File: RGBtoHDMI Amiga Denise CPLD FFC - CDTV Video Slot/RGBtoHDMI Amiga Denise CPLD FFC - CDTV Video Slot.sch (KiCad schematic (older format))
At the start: 33 parts, among them CN10 Conn_02x15_Odd_Even, J1 Raspberry_Pi_2_3, U1 XC9572VQ44 or XC9572XL-10VQG4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

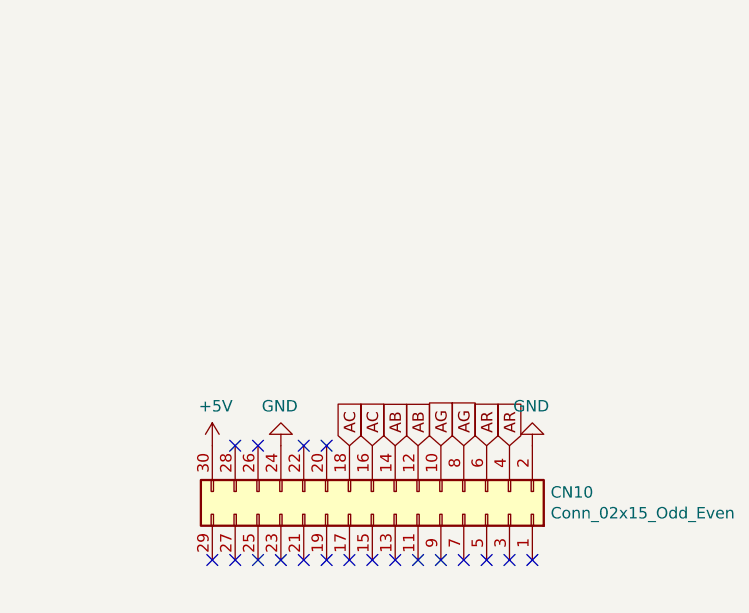
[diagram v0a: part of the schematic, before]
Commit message: Added L+R audio points
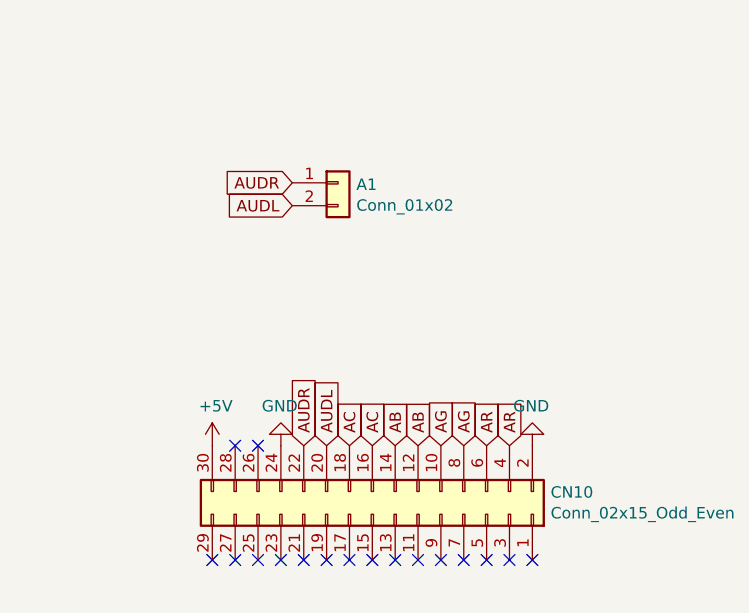
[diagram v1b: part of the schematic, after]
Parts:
- added A1: Conn_01x02, Connector_PinHeader_2.54mm:PinHeader_1x02_P2.54mm_Vertical, symbol Connector_Generic:Conn_01x02
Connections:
- net AUDL: now reaches CN10.20 (Pin_20)
- net AUDL: now also A1.2 (Pin_2)
- net AUDR: now reaches CN10.22 (Pin_22)
- net AUDR: now also A1.1 (Pin_1)
- no-connect marks 20 -> 18
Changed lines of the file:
@@
 NoConn ~ 1750 6875
 NoConn ~ 1850 6875
-NoConn ~ 2050 6875
-NoConn ~ 2150 6875
 NoConn ~ 3050 7375
 NoConn ~ 2950 7375
@@
 Text Notes 9750 5500 0    50   ~ 0
 RX
+$Comp
+L Connector_Generic:Conn_01x02 A1
+U 1 1 61AE4E78
+P 2200 5725
+F 0 "A1" H 2280 5717 50  0000 L CNN
+F 1 "Conn_01x02" H 2280 5626 50  0000 L CNN
+F 2 "Connector_PinHeader_2.54mm:PinHeader_1x02_P2.54mm_Vertical" H 2200 5725 50  0001 C CNN
+F 3 "~" H 2200 5725 50  0001 C CNN
+	1    2200 5725
+	1    0    0    -1
+$EndComp
+Text GLabel 2050 6875 1    50   Input ~ 0
+AUDR
+Text GLabel 2150 6875 1    50   Input ~ 0
+AUDL
+Text GLabel 2000 5725 0    50   Input ~ 0
+AUDR
+Text GLabel 2000 5825 0    50   Input ~ 0
+AUDL
 $EndSCHEMATC
